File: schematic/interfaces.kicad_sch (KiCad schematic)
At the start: 21 parts, among them J2 N, J3 E, J4 S, J5 W, U5 SN74LVC2G125DCUR, U6 SN74LVC2G125DCUR, U7 SN74LVC2G125DCUR, U8 SN74LVC2G125DCUR

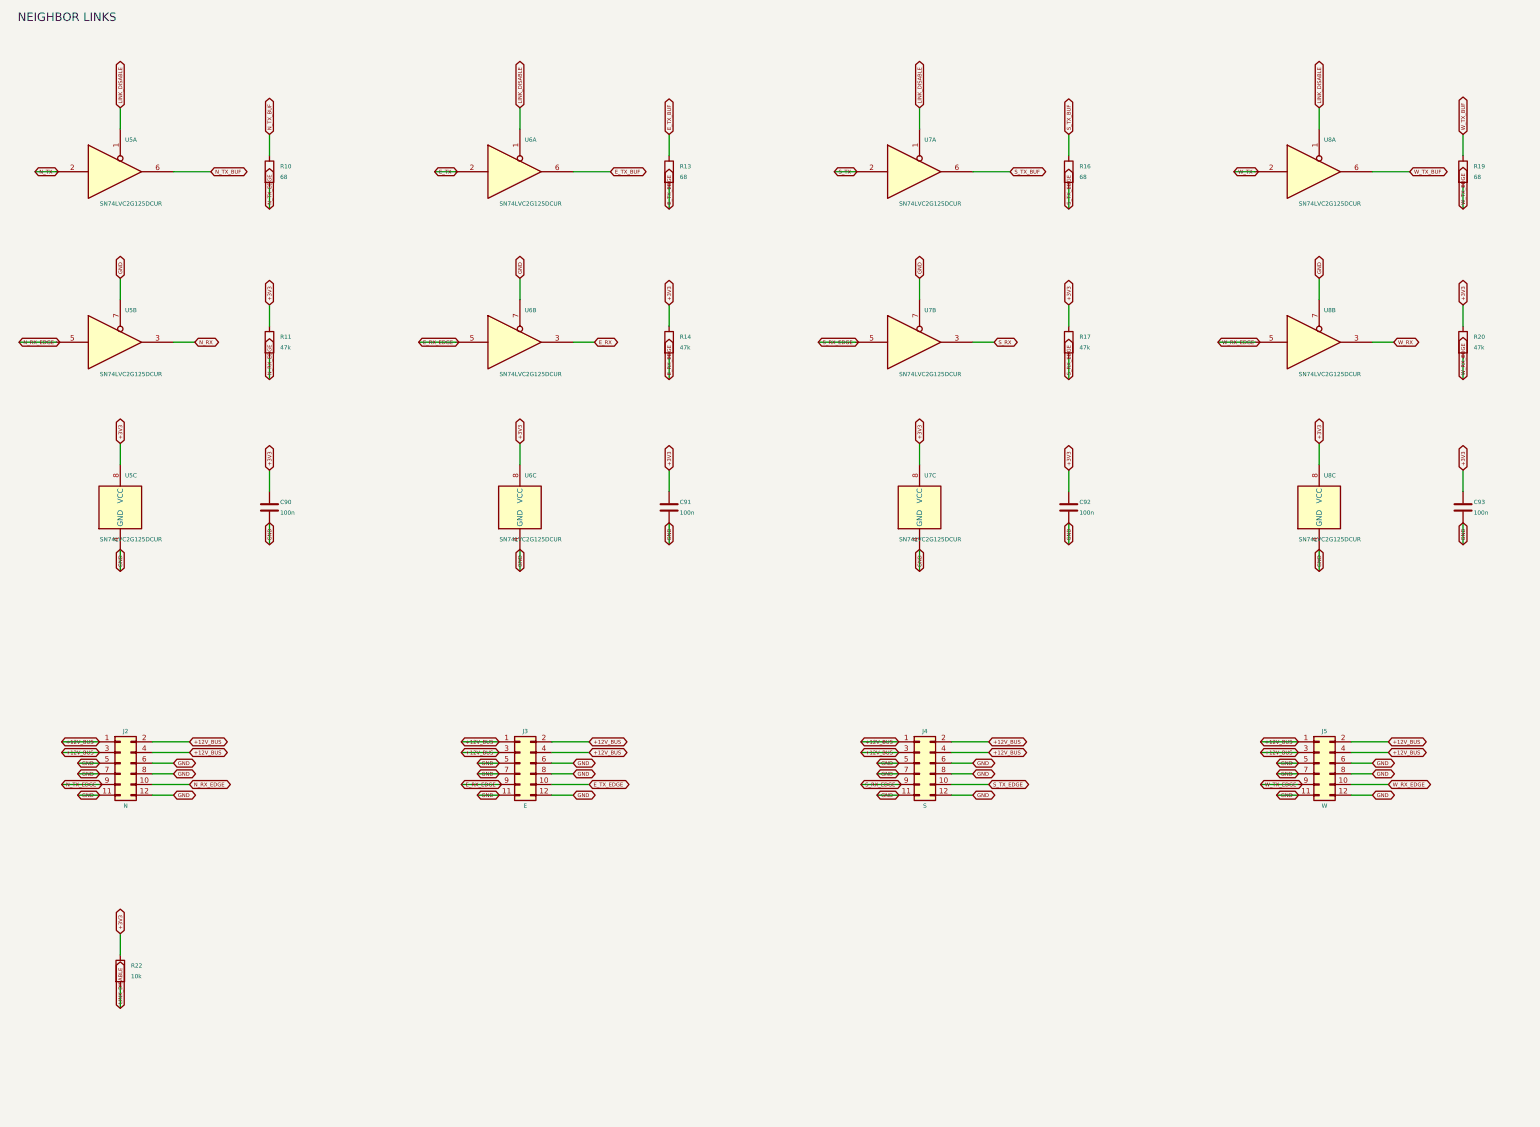
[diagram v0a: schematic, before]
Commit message: finish tile schematics and connector footprints
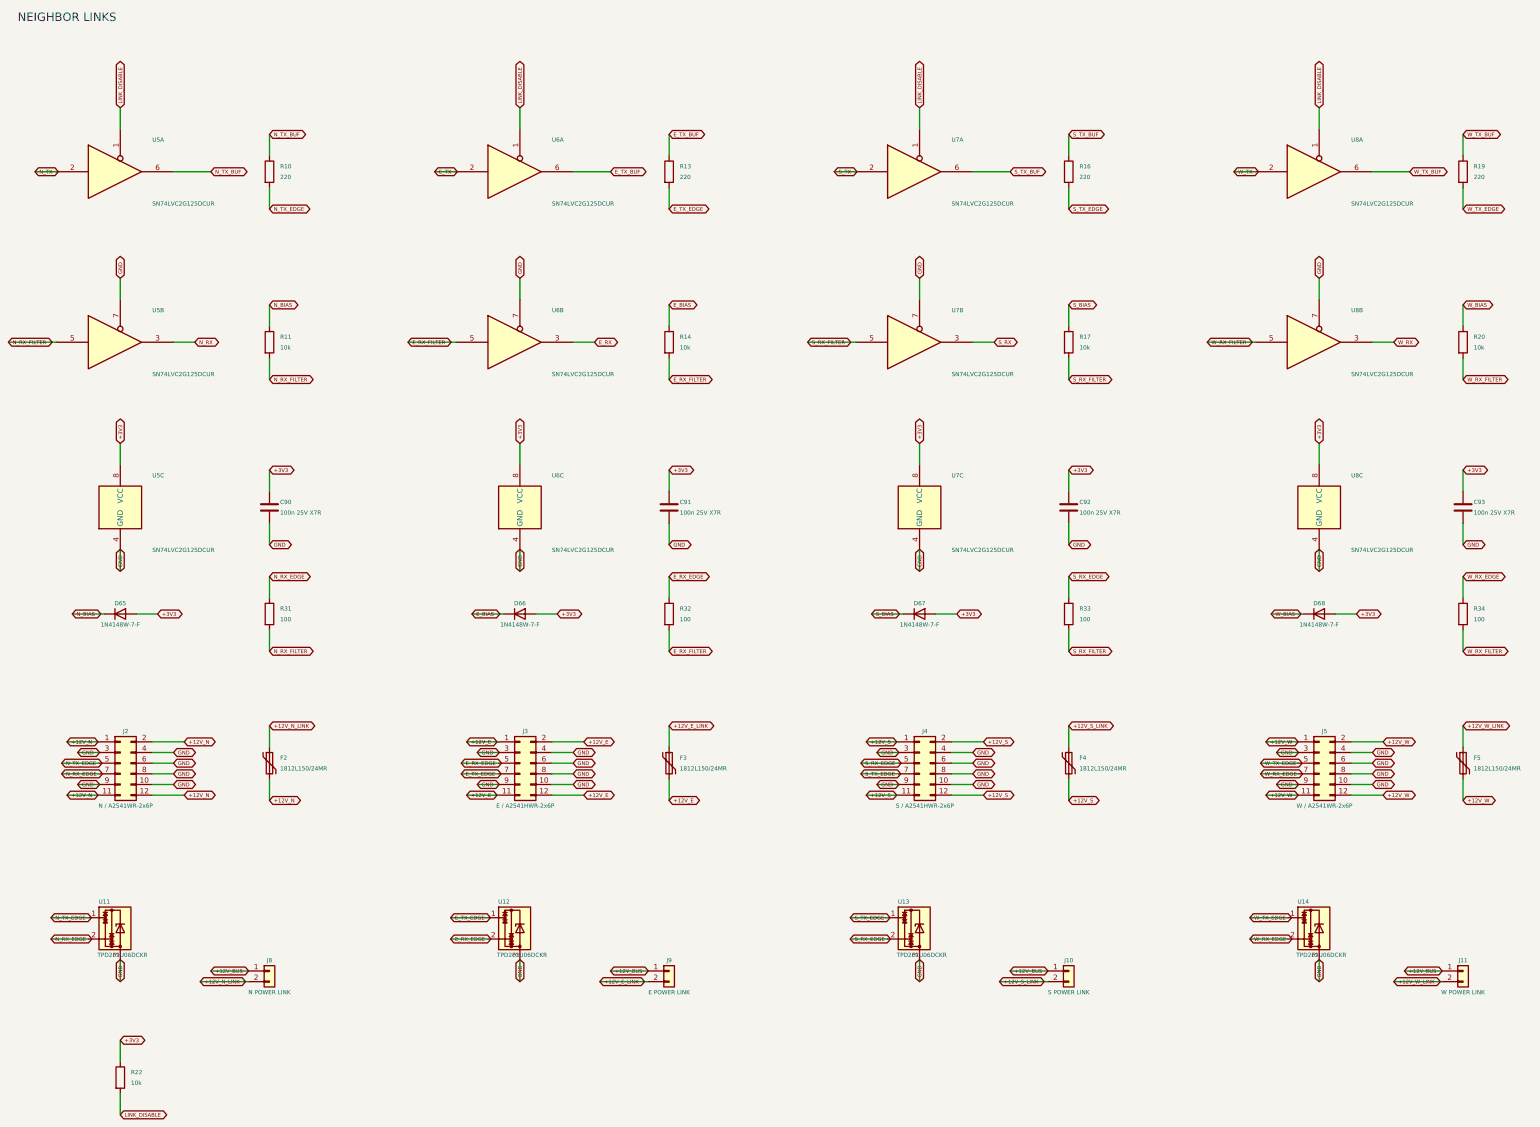
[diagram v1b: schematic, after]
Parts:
- added D65, D66, D67, D68: 1N4148W-7-F, Diode_SMD:D_SOD-123, symbol Diode:1N4148W
- added F2, F3, F4, F5: 1812L150/24MR, Fuse:Fuse_1812_4532Metric, symbol Device:Polyfuse
- added J10: S POWER LINK, Connector_PinHeader_2.54mm:PinHeader_1x02_P2.54mm_Vertical, symbol Connector_Generic:Conn_01x02
- added J11: W POWER LINK, Connector_PinHeader_2.54mm:PinHeader_1x02_P2.54mm_Vertical, symbol Connector_Generic:Conn_01x02
- added J8: N POWER LINK, Connector_PinHeader_2.54mm:PinHeader_1x02_P2.54mm_Vertical, symbol Connector_Generic:Conn_01x02
- added J9: E POWER LINK, Connector_PinHeader_2.54mm:PinHeader_1x02_P2.54mm_Vertical, symbol Connector_Generic:Conn_01x02
- added R31, R32, R33, R34: 100, Resistor_SMD:R_0603_1608Metric, symbol Device:R
- added U11, U12, U13, U14: TPD2E2U06DCKR, Package_TO_SOT_SMD:SOT-323_SC-70, symbol Power_Protection:TPD2E2U06DCK
- C90, C91, C92, C93: value 100n -> 100n 25V X7R; MPN (none) -> C0603C104K3RACTU; Manufacturer (none) -> KEMET
- J2: value N -> N / A2541WR-2x6P; footprint Connector_PinHeader_2.54mm:PinHeader_2x06_P2.54mm_Horizontal -> RGB_Tiles:CJT_A2541WR_2x06_P2.54mm_RA; MPN (none) -> A2541WR-2x6P; Manufacturer (none) -> CJT
- J3: value E -> E / A2541HWR-2x6P; footprint Connector_PinSocket_2.54mm:PinSocket_2x06_P2.54mm_Horizontal -> RGB_Tiles:CJT_A2541HWR_2x06_P2.54mm_RA; MPN (none) -> A2541HWR-2x6P; Manufacturer (none) -> CJT
- J4: value S -> S / A2541HWR-2x6P; footprint Connector_PinSocket_2.54mm:PinSocket_2x06_P2.54mm_Horizontal -> RGB_Tiles:CJT_A2541HWR_2x06_P2.54mm_RA; MPN (none) -> A2541HWR-2x6P; Manufacturer (none) -> CJT
- J5: value W -> W / A2541WR-2x6P; footprint Connector_PinHeader_2.54mm:PinHeader_2x06_P2.54mm_Horizontal -> RGB_Tiles:CJT_A2541WR_2x06_P2.54mm_RA; MPN (none) -> A2541WR-2x6P; Manufacturer (none) -> CJT
- R10, R13, R16, R19: value 68 -> 220; MPN (none) -> RC0603FR-07220RL; Manufacturer (none) -> Yageo; Power (none) -> 0.1W; Tolerance (none) -> 1%
- R11, R14, R17, R20: value 47k -> 10k; MPN (none) -> RC0603FR-0710KL; Manufacturer (none) -> Yageo; Power (none) -> 0.1W; Tolerance (none) -> 1%
- R22: MPN (none) -> RC0603FR-0710KL; Manufacturer (none) -> Yageo; Power (none) -> 0.1W; Tolerance (none) -> 1%
- U5, U6, U7, U8: footprint (none) -> Package_SO:VSSOP-8_2.3x2mm_P0.5mm; MPN (none) -> SN74LVC2G125DCUR; Manufacturer (none) -> Texas Instruments
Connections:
- net +12V_BUS: now also J10.1 (Pin_1), J11.1 (Pin_1), J8.1 (Pin_1), J9.1 (Pin_1); no longer J2.1 (Pin_1), J2.2 (Pin_2), J2.3 (Pin_3), J2.4 (Pin_4), J3.1 (Pin_1), J3.2 (Pin_2), J3.3 (Pin_3), J3.4 (Pin_4), J4.1 (Pin_1), J4.2 (Pin_2), J4.3 (Pin_3), J4.4 (Pin_4), J5.1 (Pin_1), J5.2 (Pin_2), J5.3 (Pin_3), J5.4 (Pin_4)
- net +3V3: now also D65.2 (A), D66.2 (A), D67.2 (A), D68.2 (A); no longer R11.1, R14.1, R17.1, R20.1
- net E_RX_EDGE: now also J3.5 (Pin_5), R32.1, U12.2; no longer J3.9 (Pin_9), R14.2, U6.5
- net E_TX_EDGE: now also J3.7 (Pin_7), U12.1; no longer J3.10 (Pin_10)
- net GND: now also J2.10 (Pin_10), J2.3 (Pin_3), J2.4 (Pin_4), J2.9 (Pin_9), J3.10 (Pin_10), J3.3 (Pin_3), J3.4 (Pin_4), J3.9 (Pin_9), J4.10 (Pin_10), J4.3 (Pin_3), J4.4 (Pin_4), J4.9 (Pin_9), J5.10 (Pin_10), J5.3 (Pin_3), J5.4 (Pin_4), J5.9 (Pin_9), U11.3, U12.3, U13.3, U14.3; no longer J2.11 (Pin_11), J2.12 (Pin_12), J2.5 (Pin_5), J2.7 (Pin_7), J3.11 (Pin_11), J3.12 (Pin_12), J3.5 (Pin_5), J3.7 (Pin_7), J4.11 (Pin_11), J4.12 (Pin_12), J4.5 (Pin_5), J4.7 (Pin_7), J5.11 (Pin_11), J5.12 (Pin_12), J5.5 (Pin_5), J5.7 (Pin_7)
- net N_RX_EDGE: now also J2.7 (Pin_7), R31.1, U11.2; no longer J2.10 (Pin_10), R11.2, U5.5
- net N_TX_EDGE: now also J2.5 (Pin_5), U11.1; no longer J2.9 (Pin_9)
- net S_RX_EDGE: now also J4.5 (Pin_5), R33.1, U13.2; no longer J4.9 (Pin_9), R17.2, U7.5
- net S_TX_EDGE: now also J4.7 (Pin_7), U13.1; no longer J4.10 (Pin_10)
- net W_RX_EDGE: now also J5.7 (Pin_7), R34.1, U14.2; no longer J5.10 (Pin_10), R20.2, U8.5
- net W_TX_EDGE: now also J5.5 (Pin_5), U14.1; no longer J5.9 (Pin_9)
- new net +12V_E: F3.2, J3.1 (Pin_1), J3.11 (Pin_11), J3.12 (Pin_12), J3.2 (Pin_2)
- new net +12V_E_LINK: F3.1, J9.2 (Pin_2)
- new net +12V_N: F2.2, J2.1 (Pin_1), J2.11 (Pin_11), J2.12 (Pin_12), J2.2 (Pin_2)
- new net +12V_N_LINK: F2.1, J8.2 (Pin_2)
- new net +12V_S: F4.2, J4.1 (Pin_1), J4.11 (Pin_11), J4.12 (Pin_12), J4.2 (Pin_2)
- new net +12V_S_LINK: F4.1, J10.2 (Pin_2)
- new net +12V_W: F5.2, J5.1 (Pin_1), J5.11 (Pin_11), J5.12 (Pin_12), J5.2 (Pin_2)
- new net +12V_W_LINK: F5.1, J11.2 (Pin_2)
- new net E_BIAS: D66.1 (K), R14.1
- new net E_RX_FILTER: R14.2, R32.2, U6.5
- new net N_BIAS: D65.1 (K), R11.1
- new net N_RX_FILTER: R11.2, R31.2, U5.5
- new net S_BIAS: D67.1 (K), R17.1
- new net S_RX_FILTER: R17.2, R33.2, U7.5
- new net W_BIAS: D68.1 (K), R20.1
- new net W_RX_FILTER: R20.2, R34.2, U8.5
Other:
- moved on the sheet: R22

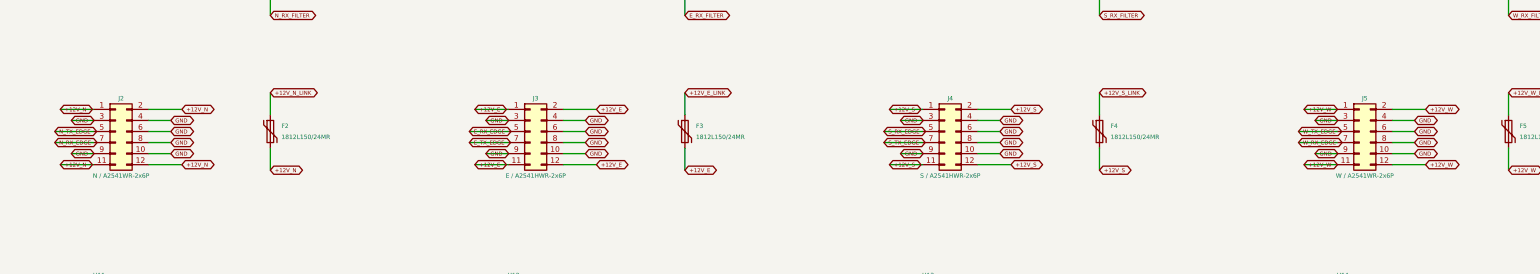
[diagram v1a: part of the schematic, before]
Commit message: place tile components and route led data chain
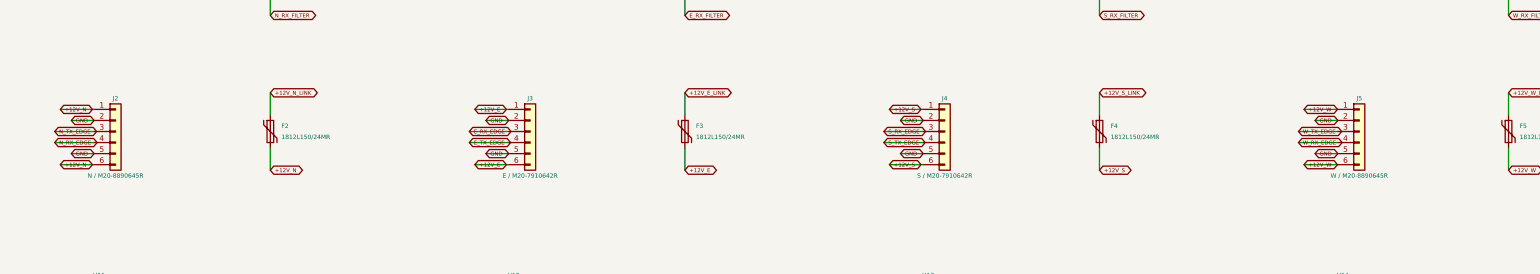
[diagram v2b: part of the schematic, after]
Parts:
- J2: value N / A2541WR-2x6P -> N / M20-8890645R; footprint RGB_Tiles:CJT_A2541WR_2x06_P2.54mm_RA -> RGB_Tiles:Harwin_M20-8890645R_1x06_RA_SMD; symbol Connector_Generic:Conn_02x06_Odd_Even -> Connector_Generic:Conn_01x06; MPN A2541WR-2x6P -> M20-8890645R; Manufacturer CJT -> Harwin
- J3: value E / A2541HWR-2x6P -> E / M20-7910642R; footprint RGB_Tiles:CJT_A2541HWR_2x06_P2.54mm_RA -> RGB_Tiles:Harwin_M20-7910642R_1x06_RA_SMD; symbol Connector_Generic:Conn_02x06_Odd_Even -> Connector_Generic:Conn_01x06; MPN A2541HWR-2x6P -> M20-7910642R; Manufacturer CJT -> Harwin
- J4: value S / A2541HWR-2x6P -> S / M20-7910642R; footprint RGB_Tiles:CJT_A2541HWR_2x06_P2.54mm_RA -> RGB_Tiles:Harwin_M20-7910642R_1x06_RA_SMD; symbol Connector_Generic:Conn_02x06_Odd_Even -> Connector_Generic:Conn_01x06; MPN A2541HWR-2x6P -> M20-7910642R; Manufacturer CJT -> Harwin
- J5: value W / A2541WR-2x6P -> W / M20-8890645R; footprint RGB_Tiles:CJT_A2541WR_2x06_P2.54mm_RA -> RGB_Tiles:Harwin_M20-8890645R_1x06_RA_SMD; symbol Connector_Generic:Conn_02x06_Odd_Even -> Connector_Generic:Conn_01x06; MPN A2541WR-2x6P -> M20-8890645R; Manufacturer CJT -> Harwin
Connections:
- net +12V_E: now also J3.6 (Pin_6); no longer J3.11 (Pin_11), J3.12 (Pin_12), J3.2 (Pin_2)
- net +12V_N: now also J2.6 (Pin_6); no longer J2.11 (Pin_11), J2.12 (Pin_12), J2.2 (Pin_2)
- net +12V_S: now also J4.6 (Pin_6); no longer J4.11 (Pin_11), J4.12 (Pin_12), J4.2 (Pin_2)
- net +12V_W: now also J5.6 (Pin_6); no longer J5.11 (Pin_11), J5.12 (Pin_12), J5.2 (Pin_2)
- net E_RX_EDGE: now also J3.3 (Pin_3); no longer J3.5 (Pin_5)
- net E_TX_EDGE: now also J3.4 (Pin_4); no longer J3.7 (Pin_7)
- net GND: now also J2.2 (Pin_2), J2.5 (Pin_5), J3.2 (Pin_2), J3.5 (Pin_5), J4.2 (Pin_2), J4.5 (Pin_5), J5.2 (Pin_2), J5.5 (Pin_5); no longer J2.10 (Pin_10), J2.3 (Pin_3), J2.4 (Pin_4), J2.6 (Pin_6), J2.8 (Pin_8), J2.9 (Pin_9), J3.10 (Pin_10), J3.3 (Pin_3), J3.4 (Pin_4), J3.6 (Pin_6), J3.8 (Pin_8), J3.9 (Pin_9), J4.10 (Pin_10), J4.3 (Pin_3), J4.4 (Pin_4), J4.6 (Pin_6), J4.8 (Pin_8), J4.9 (Pin_9), J5.10 (Pin_10), J5.3 (Pin_3), J5.4 (Pin_4), J5.6 (Pin_6), J5.8 (Pin_8), J5.9 (Pin_9)
- net N_RX_EDGE: now also J2.4 (Pin_4); no longer J2.7 (Pin_7)
- net N_TX_EDGE: now also J2.3 (Pin_3); no longer J2.5 (Pin_5)
- net S_RX_EDGE: now also J4.3 (Pin_3); no longer J4.5 (Pin_5)
- net S_TX_EDGE: now also J4.4 (Pin_4); no longer J4.7 (Pin_7)
- net W_RX_EDGE: now also J5.4 (Pin_4); no longer J5.7 (Pin_7)
- net W_TX_EDGE: now also J5.3 (Pin_3); no longer J5.5 (Pin_5)

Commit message: add firmware, controller and manufacturing files
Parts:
- C90, C91, C92, C93: MPN C0603C104K3RACTU -> CL10B104KA8NNNC; Manufacturer KEMET -> Samsung Electro-Mechanics
- U11, U12, U13, U14: value TPD2E2U06DCKR -> TPD2E2U06QDCKRQ1; MPN TPD2E2U06DCKR -> TPD2E2U06QDCKRQ1
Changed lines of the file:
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@@
 			)
 		)
-		(property "Value" "TPD2E2U06DCKR"
+		(property "Value" "TPD2E2U06QDCKRQ1"
 			(at 44.958 241.3 0)
 			(effects
@@
 			)
 		)
-		(property "Datasheet" "https://www.ti.com/lit/ds/symlink/tpd2e2u06.pdf"
+		(property "Datasheet" "https://www.ti.com/lit/ds/symlink/tpd2e2u06-q1.pdf"
 			(at 44.45 234.95 0)
 			(effects
@@
 			)
 		)
-		(property "MPN" "TPD2E2U06DCKR"
+		(property "MPN" "TPD2E2U06QDCKRQ1"
 			(at 44.45 234.95 0)
 			(effects
@@
 			)
 		)
-		(property "Datasheet" "https://search.kemet.com/component-documentation/download/specsheet/C0603C104K3RACTU"
+		(property "Datasheet" "https://product.samsungsem.com/mlcc/CL10B104KA8NNN.do"
 			(at 80.01 134.62 0)
 			(effects
@@
 			)
 		)
-		(property "Manufacturer" "KEMET"
+		(property "Manufacturer" "Samsung Electro-Mechanics"
 			(at 80.01 134.62 0)
 			(effects
@@
 			)
 		)
-		(property "MPN" "C0603C104K3RACTU"
+		(property "MPN" "CL10B104KA8NNNC"
 			(at 80.01 134.62 0)
 			(effects
@@
 			)
 		)
-		(property "Value" "TPD2E2U06DCKR"
+		(property "Value" "TPD2E2U06QDCKRQ1"
 			(at 140.208 241.3 0)
 			(effects
@@
 			)
 		)
-		(property "Datasheet" "https://www.ti.com/lit/ds/symlink/tpd2e2u06.pdf"
+		(property "Datasheet" "https://www.ti.com/lit/ds/symlink/tpd2e2u06-q1.pdf"
 			(at 139.7 234.95 0)
 			(effects
@@
 			)
 		)
-		(property "MPN" "TPD2E2U06DCKR"
+		(property "MPN" "TPD2E2U06QDCKRQ1"
 			(at 139.7 234.95 0)
 			(effects
@@
 			)
 		)
-		(property "Datasheet" "https://search.kemet.com/component-documentation/download/specsheet/C0603C104K3RACTU"
+		(property "Datasheet" "https://product.samsungsem.com/mlcc/CL10B104KA8NNN.do"
 			(at 175.26 134.62 0)
 			(effects
@@
 			)
 		)
-		(property "Manufacturer" "KEMET"
+		(property "Manufacturer" "Samsung Electro-Mechanics"
 			(at 175.26 134.62 0)
 			(effects
@@
 			)
 		)
-		(property "MPN" "C0603C104K3RACTU"
+		(property "MPN" "CL10B104KA8NNNC"
 			(at 175.26 134.62 0)
 			(effects
@@
 			)
 		)
-		(property "Value" "TPD2E2U06DCKR"
+		(property "Value" "TPD2E2U06QDCKRQ1"
 			(at 235.458 241.3 0)
 			(effects
@@
 			)
 		)
-		(property "Datasheet" "https://www.ti.com/lit/ds/symlink/tpd2e2u06.pdf"
+		(property "Datasheet" "https://www.ti.com/lit/ds/symlink/tpd2e2u06-q1.pdf"
 			(at 234.95 234.95 0)
 			(effects
@@
 			)
 		)
-		(property "MPN" "TPD2E2U06DCKR"
+		(property "MPN" "TPD2E2U06QDCKRQ1"
 			(at 234.95 234.95 0)
 			(effects
@@
 			)
 		)
-		(property "Datasheet" "https://search.kemet.com/component-documentation/download/specsheet/C0603C104K3RACTU"
+		(property "Datasheet" "https://product.samsungsem.com/mlcc/CL10B104KA8NNN.do"
 			(at 270.51 134.62 0)
 			(effects
@@
 			)
 		)
-		(property "Manufacturer" "KEMET"
+		(property "Manufacturer" "Samsung Electro-Mechanics"
 			(at 270.51 134.62 0)
 			(effects
@@
 			)
 		)
-		(property "MPN" "C0603C104K3RACTU"
+		(property "MPN" "CL10B104KA8NNNC"
 			(at 270.51 134.62 0)
 			(effects
@@
 			)
 		)
-		(property "Value" "TPD2E2U06DCKR"
+		(property "Value" "TPD2E2U06QDCKRQ1"
 			(at 330.708 241.3 0)
 			(effects
@@
 			)
 		)
-		(property "Datasheet" "https://www.ti.com/lit/ds/symlink/tpd2e2u06.pdf"
+		(property "Datasheet" "https://www.ti.com/lit/ds/symlink/tpd2e2u06-q1.pdf"
 			(at 330.2 234.95 0)
 			(effects
@@
 			)
 		)
-		(property "MPN" "TPD2E2U06DCKR"
+		(property "MPN" "TPD2E2U06QDCKRQ1"
 			(at 330.2 234.95 0)
 			(effects
@@
 			)
 		)
-		(property "Datasheet" "https://search.kemet.com/component-documentation/download/specsheet/C0603C104K3RACTU"
+		(property "Datasheet" "https://product.samsungsem.com/mlcc/CL10B104KA8NNN.do"
 			(at 364.49 134.62 0)
 			(effects
@@
 			)
 		)
-		(property "Manufacturer" "KEMET"
+		(property "Manufacturer" "Samsung Electro-Mechanics"
 			(at 364.49 134.62 0)
 			(effects
@@
 			)
 		)
-		(property "MPN" "C0603C104K3RACTU"
+		(property "MPN" "CL10B104KA8NNNC"
 			(at 364.49 134.62 0)
 			(effects
